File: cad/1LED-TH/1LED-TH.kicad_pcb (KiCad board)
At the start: 2 copper layers, 28.4 x 15.2 mm, 3 parts, among them J1 Screw_Terminal_01x02

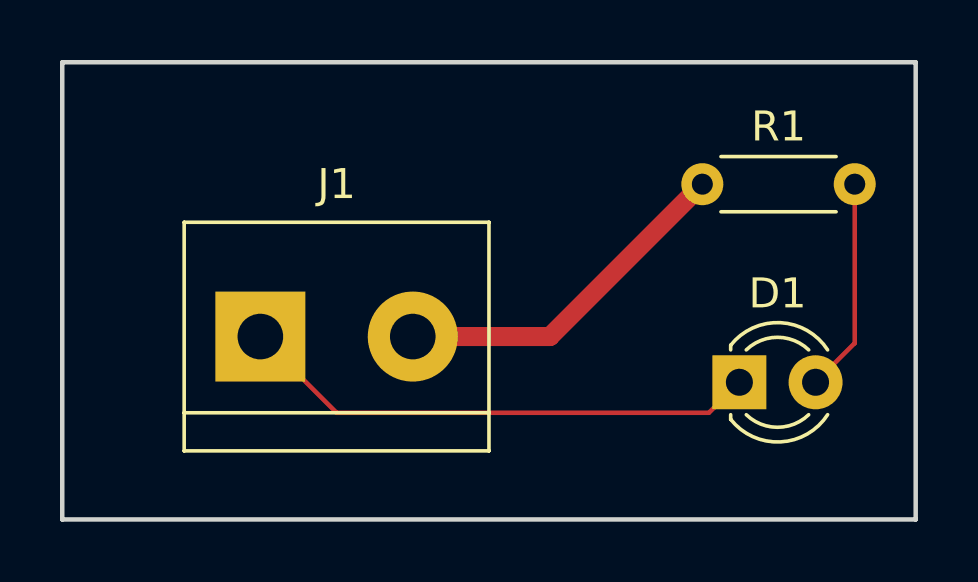
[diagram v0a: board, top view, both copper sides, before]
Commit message: added mounting holes
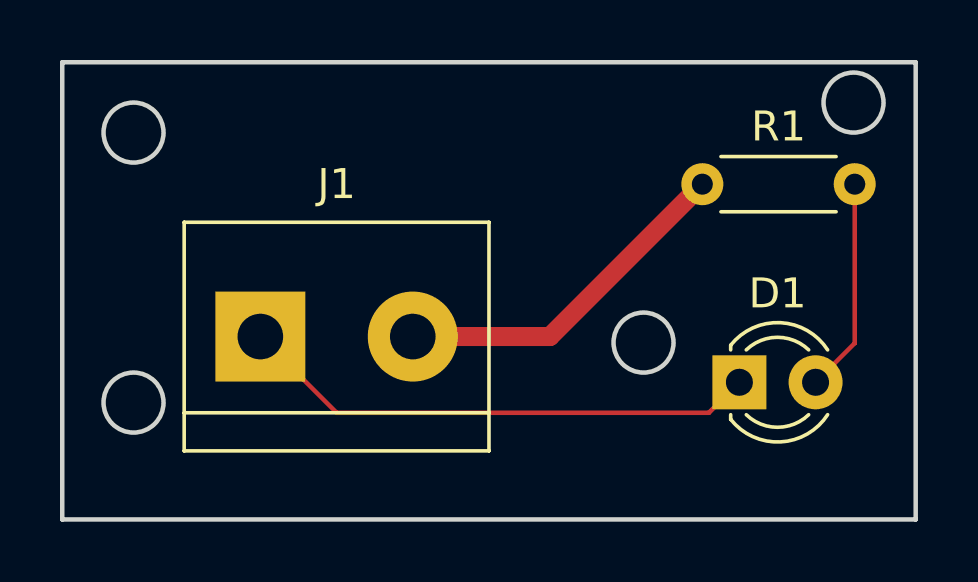
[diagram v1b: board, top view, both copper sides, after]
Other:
- outline, holes or cut-outs redrawn
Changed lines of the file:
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@@
       (effects (font (size 1 1) (thickness 0.15)))
     )
-    (fp_text value "Screw_Terminal_01x02" (at 2.54 5.08) (layer "F.Fab")
+    (fp_text value "Screw_Terminal_01x02" (at 4.572 5.08) (layer "F.Fab")
       (effects (font (size 1 1) (thickness 0.15)))
     )
@@
     )
   )
+  (gr_circle (center 42 180) (end 42 179) (layer "Edge.Cuts") (width 0.15) (fill none))
   (gr_poly
     (pts
@@
       (xy 68.072 168.656)
     ) (layer "Edge.Cuts") (width 0.15) (fill none))
+  (gr_circle (center 66 170) (end 66 169) (layer "Edge.Cuts") (width 0.15) (fill none))
+  (gr_circle (center 42 171) (end 42 170) (layer "Edge.Cuts") (width 0.15) (fill none))
+  (gr_circle (center 59 178) (end 59 177) (layer "Edge.Cuts") (width 0.15) (fill none))
   (segment (start 48.768 180.34) (end 46.228 177.8) (width 0.1524) (layer "F.Cu") (net 1))
   (segment (start 62.195 179.324) (end 61.179 180.34) (width 0.1524) (layer "F.Cu") (net 1))
